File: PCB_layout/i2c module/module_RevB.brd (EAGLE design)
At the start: 33.3 x 50 mm, 17 parts, among them IC1 ATTINY85-20SU, J1 M20-9980346, P1 PROTO_VIAS_01X01-1.2

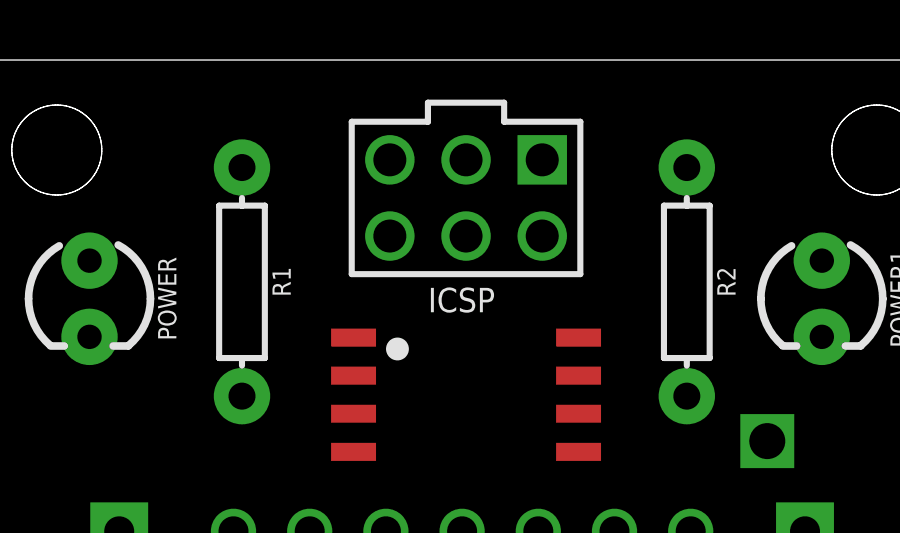
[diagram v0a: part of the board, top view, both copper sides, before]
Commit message: added decoupling cap to VCC/GND line
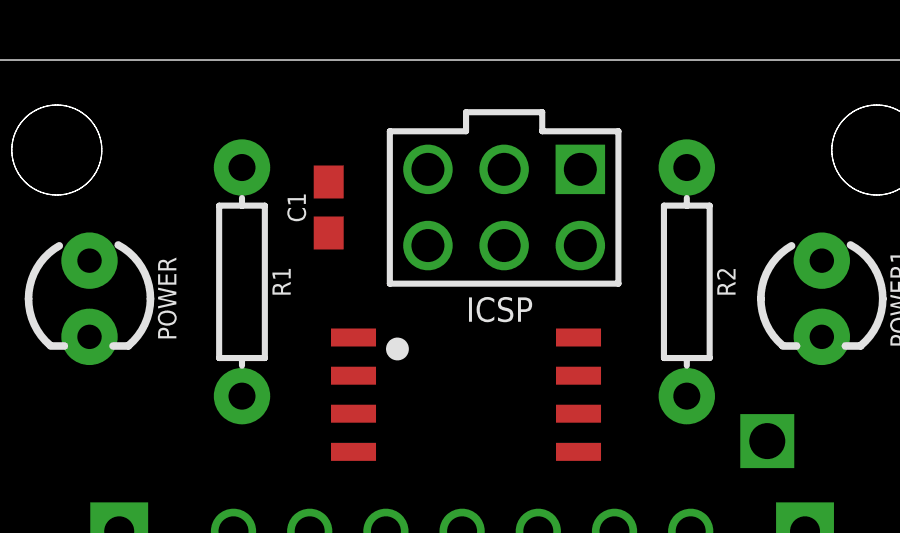
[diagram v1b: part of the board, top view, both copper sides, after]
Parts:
- added C1: 0.1uF, SparkFun-Capacitors:0603
- moved J1 1.31 mm to (17.9, 42.5)
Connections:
- net GND: now also C1.1
- net VCC: now also C1.2
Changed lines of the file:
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@@
 <?xml version="1.0" encoding="utf-8"?>
 <!DOCTYPE eagle SYSTEM "eagle.dtd">
-<eagle version="9.0.1">
+<eagle version="9.1.1">
 <drawing>
 <settings>
@@
 <param name="checkStop" value="0"/>
 <param name="checkValues" value="0"/>
+<param name="checkNames" value="1"/>
+<param name="checkWireStubs" value="1"/>
+<param name="checkPolygonWidth" value="0"/>
 <param name="useDiameter" value="13"/>
 <param name="maxErrors" value="50"/>
@@
 <element name="U$2" library="BadgeParts" package="7X-PADS-NC" value="7X-PADS-NC" x="8.89" y="19.05"/>
 <element name="5" library="BadgeParts" package="3X-PADS" value="3X-PADS-CONNECTED" x="22.86" y="16.51"/>
-<element name="J1" library="BadgeParts" package="HDRV6W64P254_2X3_762X508X868P" value="M20-9980346" x="16.6409375" y="42.8625">
-<attribute name="ARROW_PART_NUMBER" value="M20-9980346" x="16.6409375" y="42.8625" size="1.778" layer="27" display="off"/>
-<attribute name="ARROW_PRICE/STOCK" value="http://uk.rs-online.com/web/p/products/7457046P" x="16.6409375" y="42.8625" size="1.778" layer="27" display="off"/>
-<attribute name="DESCRIPTION" value="03+03 DIL Vertical Pin Header HARWIN M20 Series, 2.54mm Pitch 6 Way 2 Row Straight PCB Header, Solder Termination, 3A" x="16.6409375" y="42.8625" size="1.778" layer="27" display="off"/>
-<attribute name="HEIGHT" value="8.68mm" x="16.6409375" y="42.8625" size="1.778" layer="27" display="off"/>
-<attribute name="MANUFACTURER_NAME" value="HARWIN" x="16.6409375" y="42.8625" size="1.778" layer="27" display="off"/>
-<attribute name="MANUFACTURER_PART_NUMBER" value="M20-9980346" x="16.6409375" y="42.8625" size="1.778" layer="27" display="off"/>
-<attribute name="RS_PART_NUMBER" value="7457046P" x="16.6409375" y="42.8625" size="1.778" layer="27" display="off"/>
-<attribute name="RS_PRICE/STOCK" value="http://uk.rs-online.com/web/p/products/7457046P" x="16.6409375" y="42.8625" size="1.778" layer="27" display="off"/>
+<element name="J1" library="BadgeParts" package="HDRV6W64P254_2X3_762X508X868P" value="M20-9980346" x="17.9109375" y="42.545">
+<attribute name="ARROW_PART_NUMBER" value="M20-9980346" x="17.9109375" y="42.545" size="1.778" layer="27" display="off"/>
+<attribute name="ARROW_PRICE/STOCK" value="http://uk.rs-online.com/web/p/products/7457046P" x="17.9109375" y="42.545" size="1.778" layer="27" display="off"/>
+<attribute name="DESCRIPTION" value="03+03 DIL Vertical Pin Header HARWIN M20 Series, 2.54mm Pitch 6 Way 2 Row Straight PCB Header, Solder Termination, 3A" x="17.9109375" y="42.545" size="1.778" layer="27" display="off"/>
+<attribute name="HEIGHT" value="8.68mm" x="17.9109375" y="42.545" size="1.778" layer="27" display="off"/>
+<attribute name="MANUFACTURER_NAME" value="HARWIN" x="17.9109375" y="42.545" size="1.778" layer="27" display="off"/>
+<attribute name="MANUFACTURER_PART_NUMBER" value="M20-9980346" x="17.9109375" y="42.545" size="1.778" layer="27" display="off"/>
+<attribute name="RS_PART_NUMBER" value="7457046P" x="17.9109375" y="42.545" size="1.778" layer="27" display="off"/>
+<attribute name="RS_PRICE/STOCK" value="http://uk.rs-online.com/web/p/products/7457046P" x="17.9109375" y="42.545" size="1.778" layer="27" display="off"/>
+</element>
+<element name="C1" library="SparkFun-Capacitors" library_urn="urn:adsk.eagle:library:510" package="0603" package3d_urn="urn:adsk.eagle:package:37414/1" value="0.1uF" x="12.065" y="45.085" rot="R90">
+<attribute name="PROD_ID" value="CAP-08604" x="12.065" y="45.085" size="1.778" layer="27" rot="R90" display="off"/>
 </element>
 </elements>
@@
 <wire x1="10.16" y1="11.43" x2="10.16" y2="13.97" width="0" layer="19" extent="1-1"/>
 <wire x1="17.8744" y1="5.6068" x2="10.16" y2="11.43" width="0" layer="19" extent="1-1"/>
-<wire x1="16.6409375" y1="44.1325" x2="17.8744" y2="5.6068" width="0" layer="19" extent="1-1"/>
+<wire x1="17.9109375" y1="43.815" x2="17.8744" y2="5.6068" width="0" layer="19" extent="1-1"/>
 </signal>
 <signal name="VCC" class="1">
@@
 <contactref element="IC1" pad="VCC"/>
 <contactref element="J1" pad="VCC"/>
+<contactref element="C1" pad="2"/>
 <wire x1="27.94" y1="31.75" x2="27.94" y2="34.29" width="0" layer="19" extent="1-1"/>
 <wire x1="27.94" y1="29.21" x2="27.94" y2="31.75" width="0" layer="19" extent="1-1"/>
@@
 <wire x1="20.8744" y1="5.6068" x2="27.94" y2="11.43" width="0" layer="19" extent="1-1"/>
 <wire x1="20.3909375" y1="40.748659375" x2="27.94" y2="34.29" width="0" layer="19" extent="1-1"/>
-<wire x1="9.173" y1="38.796" x2="20.3909375" y2="40.748659375" width="0" layer="19" extent="1-1"/>
-<wire x1="19.1809375" y1="44.1325" x2="20.8744" y2="5.6068" width="0" layer="19" extent="1-1"/>
+<wire x1="20.4509375" y1="43.815" x2="20.3909375" y2="40.748659375" width="0" layer="19" extent="1-1"/>
+<wire x1="9.173" y1="38.796" x2="20.4509375" y2="43.815" width="0" layer="19" extent="1-1"/>
+<wire x1="12.065" y1="45.935" x2="20.8744" y2="5.6068" width="0" layer="19" extent="1-1"/>
 </signal>
 <signal name="PB3">
@@
 <contactref element="IC1" pad="GND"/>
 <contactref element="J1" pad="GND"/>
-<wire x1="12.8909375" y1="36.938659375" x2="28.5" y2="40.772" width="0" layer="19" extent="1-1"/>
+<contactref element="C1" pad="1"/>
+<wire x1="15.3709375" y1="43.815" x2="28.5" y2="40.772" width="0" layer="19" extent="1-1"/>
+<wire x1="12.8909375" y1="36.938659375" x2="15.3709375" y2="43.815" width="0" layer="19" extent="1-1"/>
 <wire x1="5.08" y1="34.29" x2="12.8909375" y2="36.938659375" width="0" layer="19" extent="1-1"/>
 <wire x1="5.08" y1="31.75" x2="5.08" y2="34.29" width="0" layer="19" extent="1-1"/>
@@
 <wire x1="4.09" y1="40.772" x2="5.08" y2="34.29" width="0" layer="19" extent="1-1"/>
 <wire x1="11.8744" y1="5.6068" x2="5.08" y2="11.43" width="0" layer="19" extent="1-1"/>
-<wire x1="14.1009375" y1="44.1325" x2="11.8744" y2="5.6068" width="0" layer="19" extent="1-1"/>
+<wire x1="12.065" y1="44.235" x2="11.8744" y2="5.6068" width="0" layer="19" extent="1-1"/>
 </signal>
 <signal name="N$11">
@@
 <wire x1="15.24" y1="11.43" x2="15.24" y2="13.97" width="0" layer="19" extent="1-1"/>
 <wire x1="14.8744" y1="5.6068" x2="15.24" y2="11.43" width="0" layer="19" extent="1-1"/>
-<wire x1="16.6409375" y1="46.6725" x2="14.8744" y2="5.6068" width="0" layer="19" extent="1-1"/>
+<wire x1="17.9109375" y1="46.355" x2="14.8744" y2="5.6068" width="0" layer="19" extent="1-1"/>
 </signal>
 <signal name="N$1">
@@
 <wire x1="22.86" y1="13.97" x2="22.86" y2="16.51" width="0" layer="19" extent="1-1"/>
 <wire x1="22.86" y1="11.43" x2="22.86" y2="13.97" width="0" layer="19" extent="1-1"/>
-<wire x1="14.1009375" y1="46.6725" x2="22.86" y2="11.43" width="0" layer="19" extent="1-1"/>
+<wire x1="15.3709375" y1="46.355" x2="22.86" y2="11.43" width="0" layer="19" extent="1-1"/>
 </signal>
 <signal name="PB1">
@@
 <wire x1="12.7" y1="13.97" x2="12.7" y2="16.51" width="0" layer="19" extent="1-1"/>
 <wire x1="12.7" y1="11.43" x2="12.7" y2="13.97" width="0" layer="19" extent="1-1"/>
-<wire x1="19.1809375" y1="46.6725" x2="12.7" y2="11.43" width="0" layer="19" extent="1-1"/>
+<wire x1="20.4509375" y1="46.355" x2="12.7" y2="11.43" width="0" layer="19" extent="1-1"/>
 </signal>
 </signals>
+<mfgpreviewcolors>
+<mfgpreviewcolor name="soldermaskcolor" color="0xC8008000"/>
+<mfgpreviewcolor name="silkscreencolor" color="0xFFFEFEFE"/>
+<mfgpreviewcolor name="backgroundcolor" color="0xFF282828"/>
+<mfgpreviewcolor name="coppercolor" color="0xFFFFBF00"/>
+<mfgpreviewcolor name="substratecolor" color="0xFF786E46"/>
+</mfgpreviewcolors>
 </board>
 </drawing>
